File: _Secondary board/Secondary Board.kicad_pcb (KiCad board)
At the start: 4 copper layers, 48 x 48 mm, 21 parts, among them IC1 AS5600-ASOT, J2 Anemometer, J3 PINHD_1x5_Male, J5 SENSORS, U1 BME680, U2 VEML7700-TR, U3 HT7533

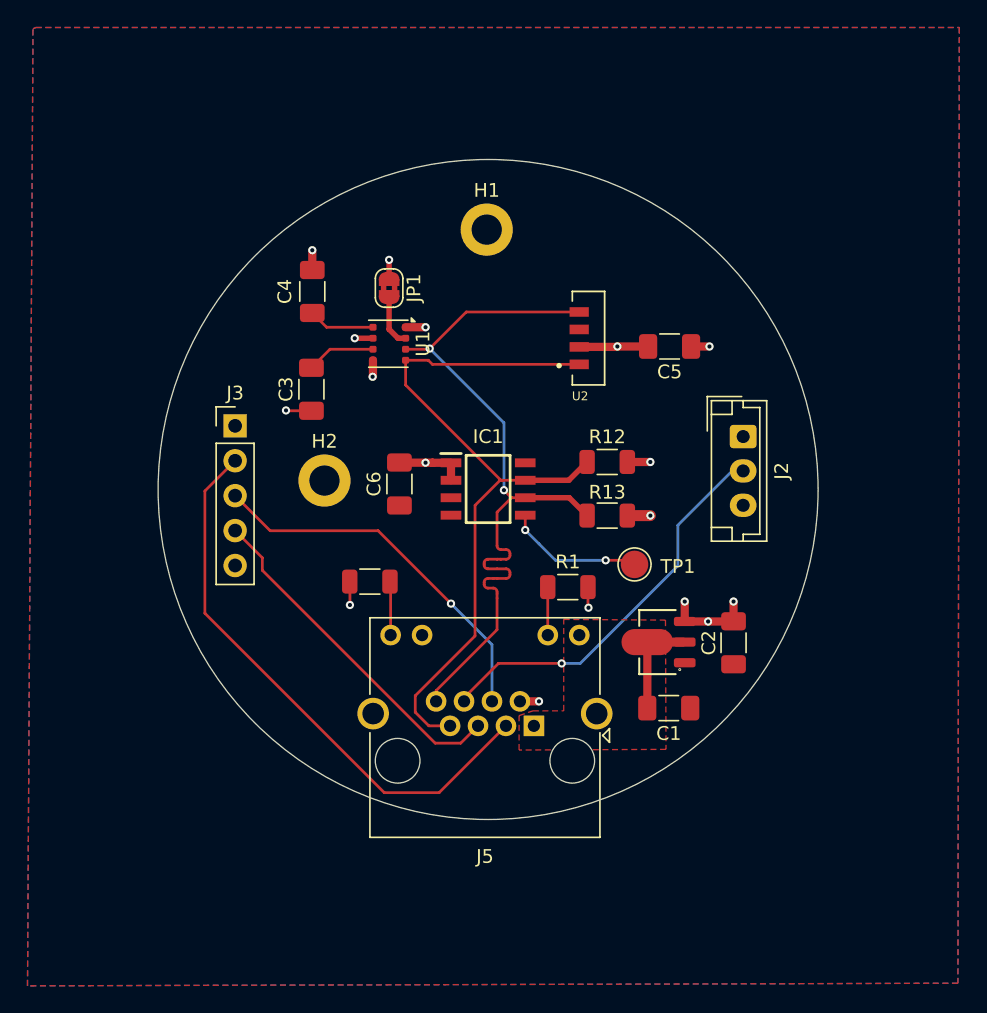
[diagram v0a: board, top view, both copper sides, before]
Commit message: Secondary Board now has the hall sensor interated Fixed BME680 schematic mistakes Updated gitignore
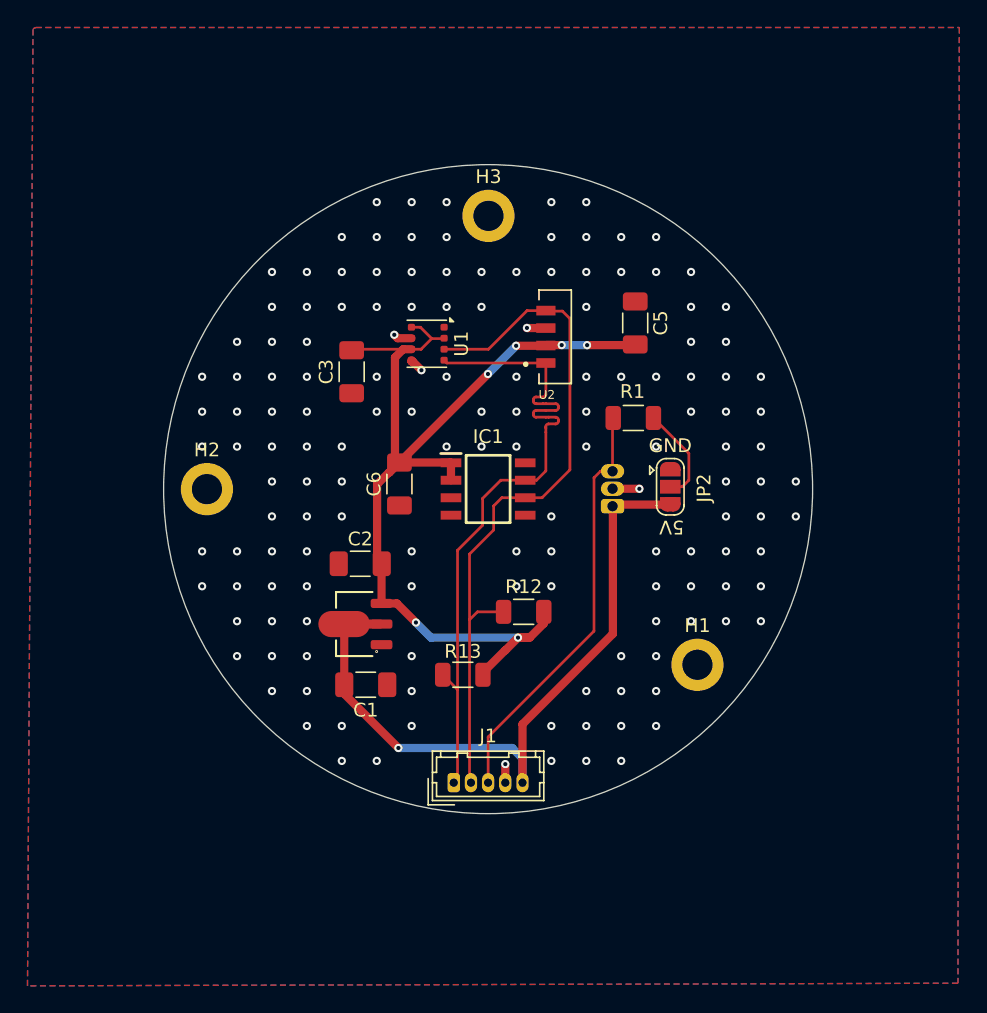
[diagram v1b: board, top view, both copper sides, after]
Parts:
- removed C4: 100nF, Capacitor_SMD:C_1206_3216Metric_Pad1.33x1.80mm_HandSolder
- removed J2: Anemometer, Connector_JST:JST_EH_B3B-EH-A_1x03_P2.50mm_Vertical
- removed J3: PINHD_1x5_Male, Connector_PinHeader_2.54mm:PinHeader_1x05_P2.54mm_Vertical
- removed J5: SENSORS, Connector_RJ:RJ45_Amphenol_RJHSE538X
- removed JP1: SolderJumper_2_Bridged, Jumper:SolderJumper-2_P1.3mm_Bridged2Bar_RoundedPad1.0x1.5mm
- removed R2: 70R, Resistor_SMD:R_1206_3216Metric
- removed TP1: TestPoint, TestPoint:TestPoint_Pad_D2.0mm
- added H3: MountingHole_M3_3.2mm_Pad, MountingHole:MountingHole_2.2mm_M2_DIN965_Pad, F.Cu at (140.0, 80.1)
- added J1: Conn_01x05_Socket, Connector_Hirose:Hirose_DF13-05P-1.25DSA_1x05_P1.25mm_Vertical, F.Cu at (137.5, 121.3)
- added JP2: SolderJumper_3_Open, Jumper:SolderJumper-3_P1.3mm_Open_RoundedPad1.0x1.5mm, F.Cu at (153.2, 99.8)
- added U4: A3144, Package_TO_SOT_THT:TO-92S, B.Cu at (149.1, 101.2)
- R1: value 150R -> 10K
- moved H1 35.2 mm to (155.2, 112.8)
- moved C2 27.8 mm to (130.7, 105.4), turned to 0 degrees
- moved C1 22.1 mm to (131.1, 114.2)
- moved U3 22.1 mm to (130.9, 109.8)
- moved R13 15.6 mm to (138.2, 113.5)
- moved R1 13.2 mm to (150.6, 94.8), turned to 180 degrees
- moved R12 12.5 mm to (142.6, 108.9)
- moved H2 8.57 mm to (119.5, 100.0)
- moved C3 3.19 mm to (130.1, 91.4)
- moved C5 3.03 mm to (150.7, 87.9), turned to -90 degrees
- moved U1 2.80 mm to (135.6, 89.4)
- moved U2 2.43 mm to (144.9, 88.9)
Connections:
- C3 pad 2: Net-(U1-VDDIO) -> +3V3
- IC1 pad 5: Net-(IC1-PGO) -> GND
- R1 pad 2: GND -> /W_SPEED
- R12 pad 1: /SCL -> /SDA
- R13 pad 1: /SDA -> /SCL
- U1 pad 2: Net-(JP1-B) -> +3V3
- U1 pad 6: Net-(U1-VDDIO) -> +3V3
- U1 pad 8: Net-(U1-VDD) -> +3V3
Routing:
- net +3V3: track 22.8 -> 73.8 mm, vias 9 -> 6
- net /+5V: track 4.82 -> 48.9 mm, vias 0 -> 1
- net /GPIO11: track 41.3 -> 0.00 mm
- net /GPIO12: track 27.3 -> 0.00 mm, vias 1 -> 0
- net /GPIO13: track 25.1 -> 0.00 mm
- net Net-(IC1-PGO): track 10.1 -> 0.00 mm, vias 2 -> 0
- net Net-(U1-VDDIO): track 5.03 -> 0.00 mm
- net Net-(U1-VDD): track 4.84 -> 0.00 mm
- net GND: track 11.8 -> 7.10 mm, vias 8 -> 149
- net /SDA: track 56.4 -> 51.8 mm, vias 2 -> 0
- net Net-(J5-Pad12): track 3.91 -> 0.00 mm
- net Net-(JP1-B): track 3.82 -> 0.00 mm
- net Net-(JP2-C): track 3.49 -> 7.14 mm
- net /SCL: track 53.7 -> 50.2 mm
- net /W_SPEED: track 29.1 -> 30.5 mm, vias 1 -> 0
- removed copper zone on In2.Cu, net +3V3
- removed copper zone on F.Cu, net /+5V
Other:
- board size 48 x 48 mm -> 47.2 x 47.2 mm
- copper layers 4 -> 2
- board text added: "5V"
- board text added: "GND"

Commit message: Replaced BME680 with BME280 Added Testpoints
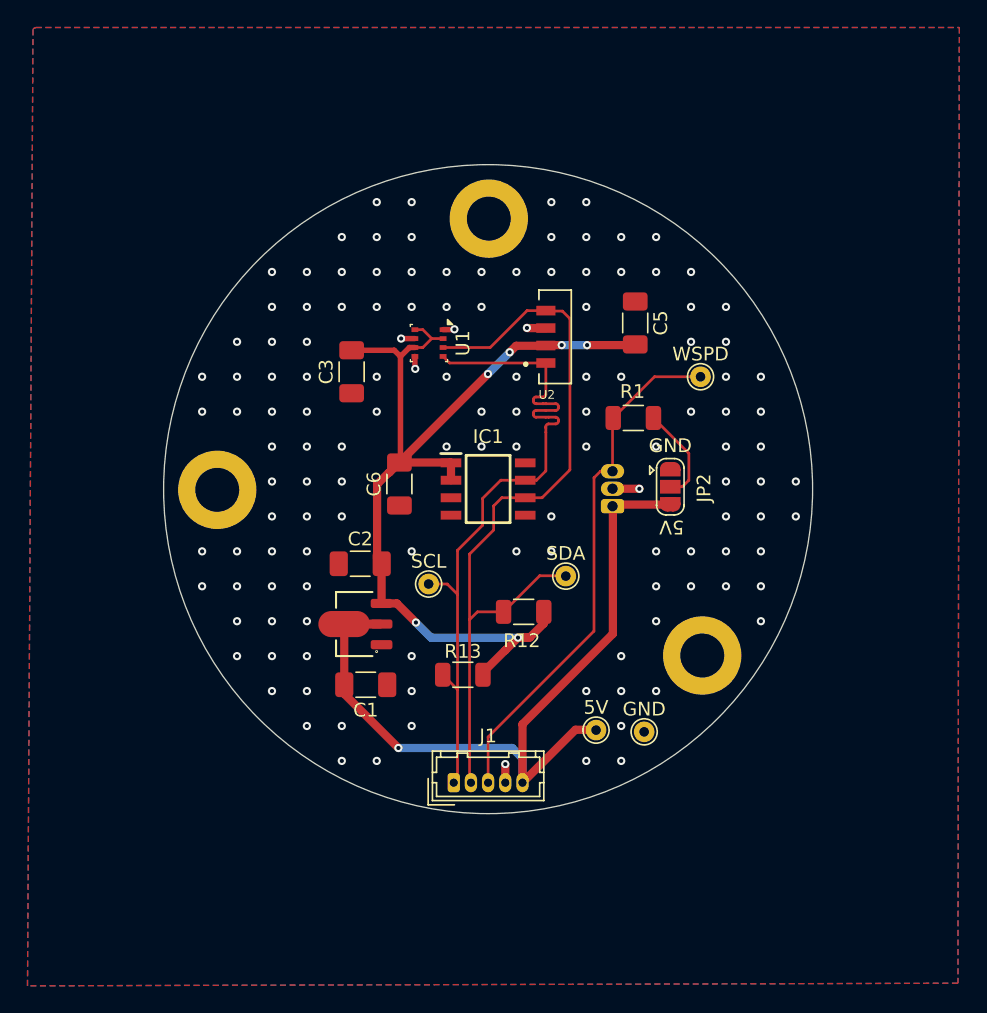
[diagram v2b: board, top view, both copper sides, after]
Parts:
- added 5V: TestPoint, TestPoint:TestPoint_THTPad_D1.5mm_Drill0.7mm, F.Cu at (147.8, 117.5)
- added GND: TestPoint, TestPoint:TestPoint_THTPad_D1.5mm_Drill0.7mm, F.Cu at (151.3, 117.6)
- added SCL: TestPoint, TestPoint:TestPoint_THTPad_D1.5mm_Drill0.7mm, F.Cu at (135.7, 106.9)
- added SDA: TestPoint, TestPoint:TestPoint_THTPad_D1.5mm_Drill0.7mm, F.Cu at (145.7, 106.3)
- added WSPD: TestPoint, TestPoint:TestPoint_THTPad_D1.5mm_Drill0.7mm, F.Cu at (155.4, 91.8)
- H1, H2, H3: footprint MountingHole:MountingHole_2.2mm_M2_DIN965_Pad -> MountingHole:MountingHole_3.2mm_M3_ISO7380_Pad
- U1: value BME680 -> BME280; footprint Package_LGA:Bosch_LGA-8_3x3mm_P0.8mm_ClockwisePinNumbering -> Package_LGA:Bosch_LGA-8_2.5x2.5mm_P0.65mm_ClockwisePinNumbering
- moved H1 0.76 mm to (155.6, 112.1)
- moved H2 0.75 mm to (120.3, 100.0)
- moved H3 0.20 mm to (140.1, 80.3)
- moved U1 0.10 mm to (135.7, 89.3)
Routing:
- net /W_SPEED: track 30.5 -> 37.4 mm
- net /+5V: track 48.9 -> 55.4 mm
- net /SDA: track 51.8 -> 57.4 mm
- net /SCL: track 50.2 -> 52.7 mm
- net +3V3: track 73.8 -> 72.5 mm
- net GND: track 7.10 -> 7.43 mm, vias 149 -> 133

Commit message: - Changed CHRG and STDBY pins to 48 and 47 (CHRG was strapping) - Exposed 5V rail do Breakout connector. Now also it matches a bme280 pinout for testing - Renamed BatteryReg net to Battery_SW - Fixed connection to 5V converter - Changed to USBLC6-2SC6 for ESD Protection - Fixed mirrored VEML7700 footprint
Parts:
- moved U2 1.45 mm to (143.4, 88.9), turned to 0 degrees
- renumbered 5V to TP-5V1, GND to TP-GND1, SCL to TP-SCL1, SDA to TP-SDA1, WSPD to TP-WSPD1
